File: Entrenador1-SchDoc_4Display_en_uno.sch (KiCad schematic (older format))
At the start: 89 parts, among them J11 CON8, J3 ICSP, J5 CON8, J6 CON8, J7 CON8, J9 3vias, P1 CONN_01X04, P10 CONN_01X04, P2 CONN_01X04, P3 CONN_01X05, P4 CONN_01X04, P5 CONN_01X09, P6 USB_B, P7 CONN_01X02, P8 CONN_01X02, P9 CONN_01X04, Q1 BC548, Q2 BC548, Q3 BC548, Q4 BC548, U1 CC56-12EWA, U2 ULN2803, U3 4511, U4 LM7805, U5 PIC18(L)F4550-I/P, Y2 20MHz

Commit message: modified:   Entrenador1-SchDoc-cache.lib 	modified:   Entrenador1-SchDoc-rescue.lib 	modified:   Entrenador1-SchDoc.bak 	modified:   Entrenador1-SchDoc.net 	modified:   Entrenador1-SchDoc.pro 	modified:   Entrenador1-SchDoc.sch 	new file:   Entrenador1-SchDoc_4Display_en_uno-cache.lib 	new file:   Entrenador1-SchDoc_4Display_en_uno.bak 	modified:   Entrenador1-SchDoc_4Display_en_uno.kicad_pcb 	modified:   Entrenador1-SchDoc_4Display_en_uno.kicad_pcb-bak 	new file:   Entrenador1-SchDoc_4Display_en_uno.net 	modified:   Entrenador1-SchDoc_4Display_en_uno.pro 	new file:   Entrenador1-SchDoc_4Display_en_uno.sch 	new file:   libreria.pretty/CA56-12EWA.kicad_mod 	modified:   libreria.pretty/TO-92_Molded_Narrow.kicad_mod 	new file:   libreria.pretty/TerminalBlock_bornier-2_P5.08mm.kicad_mod 	new file:   rescue-backup/Entrenador1-SchDoc-2019-06-22-08-57-40.pro 	new file:   rescue-backup/Entrenador1-SchDoc-2019-06-22-08-57-40.sch 	new file:   rescue-backup/Entrenador1-SchDoc-cache-2019-06-22-08-57-40.lib 	new file:   rescue-backup/Entrenador1-SchDoc-rescue-2019-06-22-08-57-40.lib 	new file:   sym-lib-table
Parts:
- removed AFF1, AFF2, AFF3, AFF4: 7SEGMENTS, libreria:7SegmentLED_LTS6760_LTS6780, symbol 7SEGMENTS
- C10, C7, C9: symbol C -> Device:C
- C11, C6, C8: symbol CP -> Device:CP
- D1, D12: symbol D -> Device:D
- D10, D11, D2, D3, D4, D5, D6, D7, D8, D9: symbol LED-RESCUE-Entrenador1-SchDoc-RESCUE-Entrenador1-SchDoc -> Entrenador1-SchDoc-rescue:LED-RESCUE-Entrenador1-SchDoc-RESCUE-Entrenador1-SchDoc
- J11, J5, J6, J7: symbol CONN_01X08 -> Entrenador1-SchDoc-rescue:CONN_01X08
- J3: symbol CONN_01X06 -> Entrenador1-SchDoc-rescue:CONN_01X06
- J9: symbol CONN_01X03 -> Entrenador1-SchDoc-rescue:CONN_01X03
- JP1: symbol JUMPER3 -> Entrenador1-SchDoc-rescue:JUMPER3
- P1, P10, P2, P4, P9: symbol CONN_01X04 -> Entrenador1-SchDoc-rescue:CONN_01X04
- P3: symbol CONN_01X05 -> Entrenador1-SchDoc-rescue:CONN_01X05
- P5: symbol CONN_01X09 -> Entrenador1-SchDoc-rescue:CONN_01X09
- P6: symbol USB_B-RESCUE-Entrenador1-SchDoc -> Entrenador1-SchDoc-rescue:USB_B-RESCUE-Entrenador1-SchDoc
- P7, P8: footprint libreria:TerminalBlock_Altech_AK300-2_P5.00mm -> Terminal_Blocks:TerminalBlock_bornier-2_P5.08mm; symbol CONN_01X02 -> Entrenador1-SchDoc-rescue:CONN_01X02
- Q1, Q2, Q3, Q4: symbol BC548 -> transistors:BC548
- R1, R10, R11, R12, R13, R14, R15, R16, R17, R18, R19, R2, R20, R21, R22, R23, R24, R25, R26, R27, R28, R29, R3, R30, R31, R32, R4, R5, R6, R7, R8, R9: symbol Res1 -> Entrenador1-SchDoc-rescue:Res1
- RV1, RV2: symbol POT-RESCUE-Entrenador1-SchDoc -> Entrenador1-SchDoc-rescue:POT-RESCUE-Entrenador1-SchDoc
- S1, S2, S3, S4, S5, S6: symbol SPST -> Entrenador1-SchDoc-rescue:SPST
- U1: symbol CC56-12EWA -> display:CC56-12EWA
- U2: symbol ULN2803 -> Entrenador1-SchDoc-rescue:ULN2803
- U3: symbol 4511 -> cmos_ieee:4511
- U4: symbol LM7805CT -> Entrenador1-SchDoc-rescue:LM7805CT
- U5: symbol PIC18(L)F4550-I/P -> Entrenador1-SchDoc-rescue:PIC18(L)F4550-I_P
- Y2: symbol XTAL -> Entrenador1-SchDoc-rescue:XTAL
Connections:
- wire segments 263 -> 289

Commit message: modified:   Entrenador1-SchDoc_4Display_en_uno.bak 	modified:   Entrenador1-SchDoc_4Display_en_uno.kicad_pcb 	modified:   Entrenador1-SchDoc_4Display_en_uno.kicad_pcb-bak 	modified:   Entrenador1-SchDoc_4Display_en_uno.net 	modified:   Entrenador1-SchDoc_4Display_en_uno.sch 	modified:   libreria.pretty/CA56-12EWA.kicad_mod 	modified:   libreria.pretty/TerminalBlock_bornier-2_P5.08mm.kicad_mod
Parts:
- P7, P8: footprint Terminal_Blocks:TerminalBlock_bornier-2_P5.08mm -> libreria:TerminalBlock_bornier-2_P5.08mm
- Q1, Q2, Q3, Q4: footprint TO_SOT_Packages_THT:TO-92_Molded_Narrow -> libreria:TO-92_Molded_Narrow
- U1: footprint Displays_7-Segment:CA56-12EWA -> libreria:CA56-12EWA
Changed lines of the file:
@@
 F 0 "Q1" H 15800 2375 50  0000 L CNN
 F 1 "BC548" H 15800 2300 50  0000 L CNN
-F 2 "TO_SOT_Packages_THT:TO-92_Molded_Narrow" H 15550 2850 50  0001 L CIN
+F 2 "libreria:TO-92_Molded_Narrow" H 15550 2850 50  0001 L CIN
 F 3 "" H 15600 2300 50  0000 L CNN
 	1    15600 2300
@@
 F 0 "Q2" H 15850 3825 50  0000 L CNN
 F 1 "BC548" H 15850 3750 50  0000 L CNN
-F 2 "TO_SOT_Packages_THT:TO-92_Molded_Narrow" H 15650 4300 50  0001 L CIN
+F 2 "libreria:TO-92_Molded_Narrow" H 15650 4300 50  0001 L CIN
 F 3 "" H 15650 3750 50  0000 L CNN
 	1    15650 3750
@@
 F 0 "Q3" H 15850 5275 50  0000 L CNN
 F 1 "BC548" H 15850 5200 50  0000 L CNN
-F 2 "TO_SOT_Packages_THT:TO-92_Molded_Narrow" H 15650 5750 50  0001 L CIN
+F 2 "libreria:TO-92_Molded_Narrow" H 15650 5750 50  0001 L CIN
 F 3 "" H 15650 5200 50  0000 L CNN
 	1    15650 5200
@@
 F 0 "Q4" H 15850 6725 50  0000 L CNN
 F 1 "BC548" H 15850 6650 50  0000 L CNN
-F 2 "TO_SOT_Packages_THT:TO-92_Molded_Narrow" H 15650 7200 50  0001 L CIN
+F 2 "libreria:TO-92_Molded_Narrow" H 15650 7200 50  0001 L CIN
 F 3 "" H 15650 6650 50  0000 L CNN
 	1    15650 6650
@@
 F 0 "P7" H 4350 4950 50  0000 C CNN
 F 1 "CONN_01X02" V 4450 4800 50  0000 C CNN
-F 2 "Terminal_Blocks:TerminalBlock_bornier-2_P5.08mm" H 4350 4800 50  0001 C CNN
+F 2 "libreria:TerminalBlock_bornier-2_P5.08mm" H 4350 4800 50  0001 C CNN
 F 3 "" H 4350 4800 50  0000 C CNN
 	1    4350 4800
@@
 F 0 "P8" H 4350 5550 50  0000 C CNN
 F 1 "CONN_01X02" V 4450 5400 50  0000 C CNN
-F 2 "Terminal_Blocks:TerminalBlock_bornier-2_P5.08mm" H 4350 5400 50  0001 C CNN
+F 2 "libreria:TerminalBlock_bornier-2_P5.08mm" H 4350 5400 50  0001 C CNN
 F 3 "" H 4350 5400 50  0000 C CNN
 	1    4350 5400
@@
 F 0 "U1" H 13650 1650 50  0000 C CNN
 F 1 "CC56-12EWA" H 15430 1650 50  0000 C CNN
-F 2 "Displays_7-Segment:CA56-12EWA" H 14600 600 50  0001 C CNN
+F 2 "libreria:CA56-12EWA" H 14600 600 50  0001 C CNN
 F 3 "" H 14220 1230 50  0001 C CNN
 	1    14600 1200

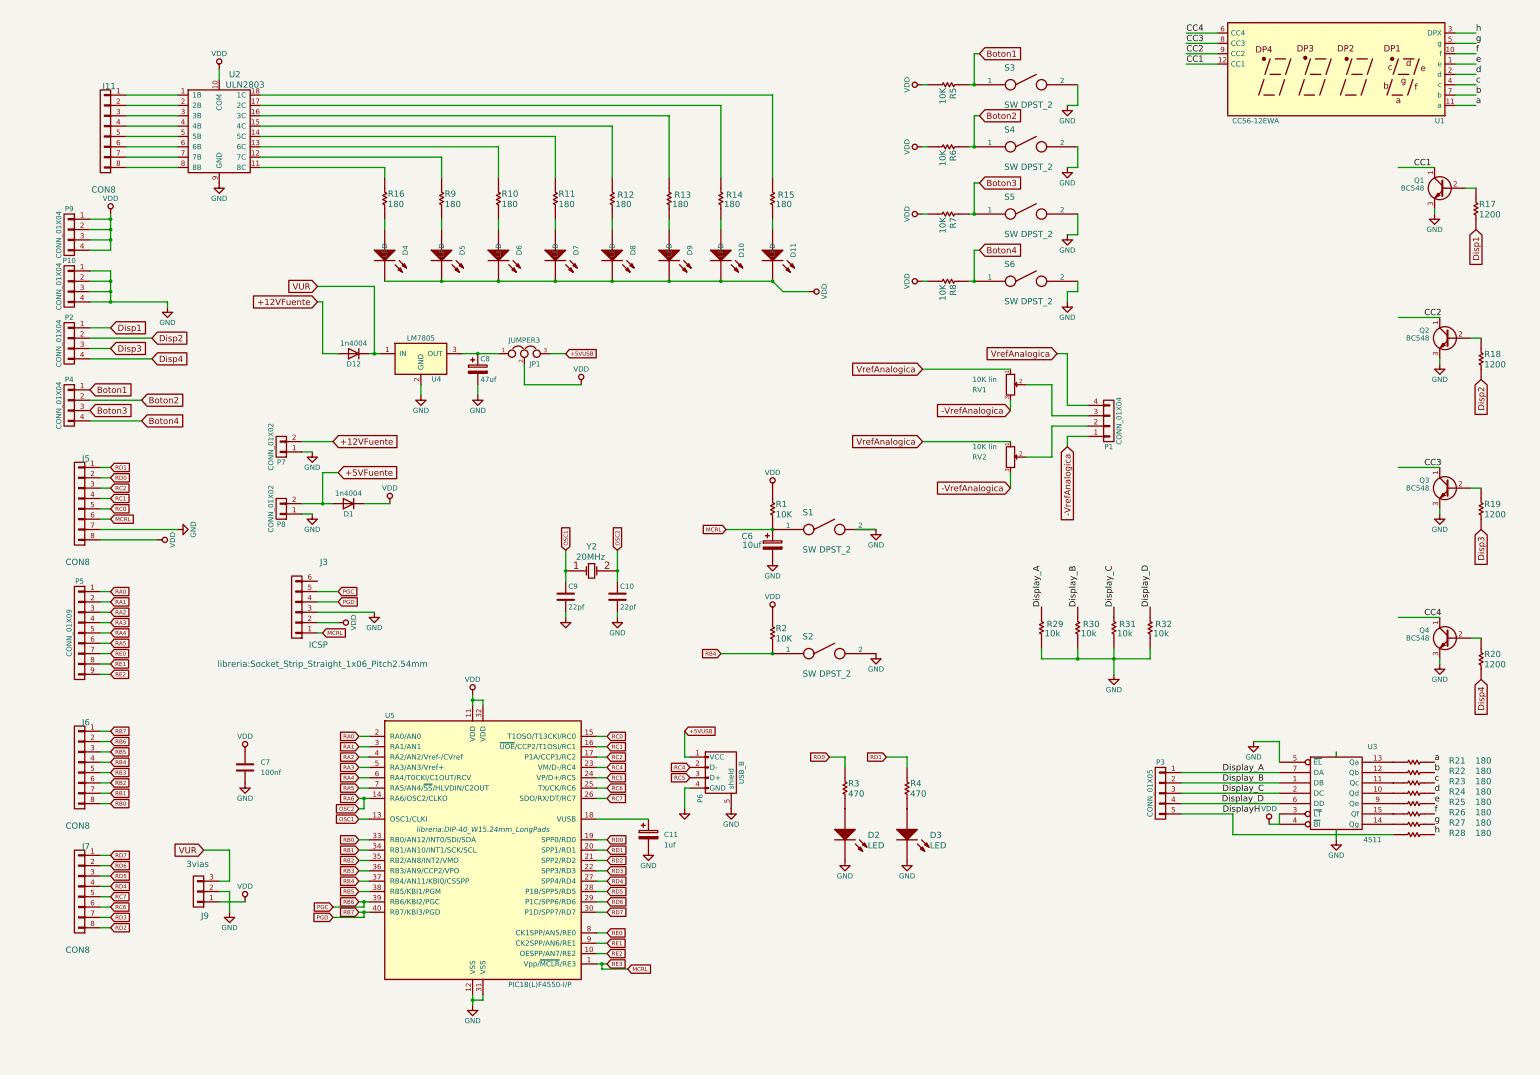
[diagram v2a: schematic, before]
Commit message: modified:   Entrenador1-SchDoc_4Display_en_uno-cache.lib 	modified:   Entrenador1-SchDoc_4Display_en_uno.bak 	modified:   Entrenador1-SchDoc_4Display_en_uno.kicad_pcb 	modified:   Entrenador1-SchDoc_4Display_en_uno.kicad_pcb-bak 	modified:   Entrenador1-SchDoc_4Display_en_uno.net 	modified:   Entrenador1-SchDoc_4Display_en_uno.sch 	modified:   libreria.pretty/TerminalBlock_bornier-2_P5.08mm.kicad_mod
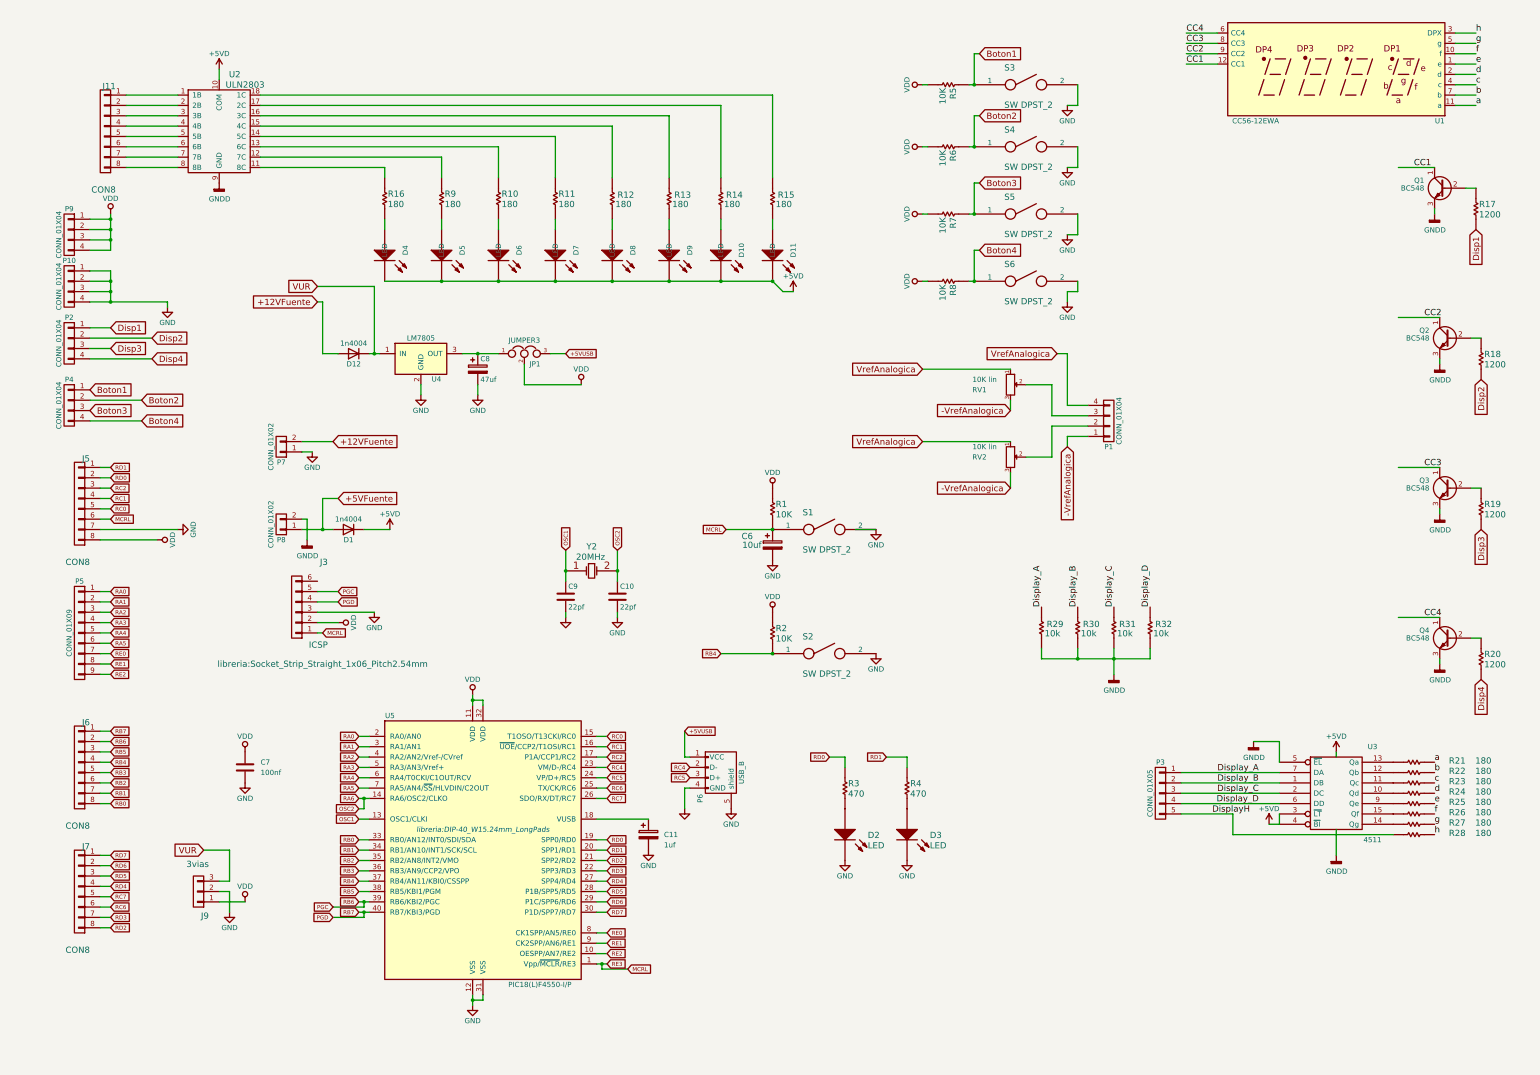
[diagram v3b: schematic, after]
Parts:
- P3: footprint Socket_Strips:Socket_Strip_Straight_1x05_Pitch2.54mm -> libreria:Socket_Strip_Straight_1x05_Pitch2.54mm
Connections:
- net +5VFuente: now also P8.1 (P1); no longer P8.2 (P2)
- net GND: no longer P8.1 (P1), Q1.3 (E), Q2.3 (E), Q3.3 (E), Q4.3 (E), R29.1, R30.1, R31.1, R32.1, U2.9 (GND), U3.5 (~EL), U3.8 (Vss)
- net VDD: no longer D1.1 (K), D10.2 (K), D11.2 (K), D4.2 (K), D5.2 (K), D6.2 (K), D7.2 (K), D8.2 (K), D9.2 (K), U2.10 (COM), U3.3 (~LT), U3.4 (~BI)
- net Vdd renamed +5VD
- net +5VD: now also D1.1 (K), D10.2 (K), D11.2 (K), D4.2 (K), D5.2 (K), D6.2 (K), D7.2 (K), D8.2 (K), D9.2 (K), U2.10 (COM), U3.3 (~LT), U3.4 (~BI)
- new net GNDD: P8.2 (P2), Q1.3 (E), Q2.3 (E), Q3.3 (E), Q4.3 (E), R29.1, R30.1, R31.1, R32.1, U2.9 (GND), U3.5 (~EL), U3.8 (Vss)
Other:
- moved on the sheet: D1, P8
